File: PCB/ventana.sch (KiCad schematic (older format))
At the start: 55 parts, among them J1 Prog, J10 CLS, J2 SW1, J3 GND, J4 SW2, J5 GND, J6 VBat, J7 Motor+, J8 Motor-, J9 GND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

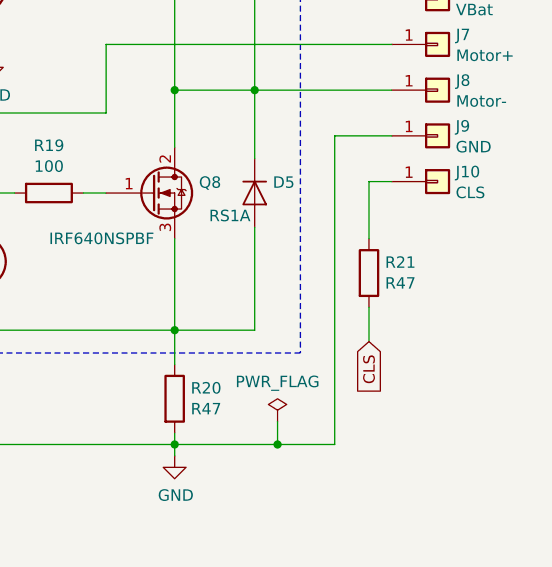
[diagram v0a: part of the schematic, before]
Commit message: Fixed a mistake in the schematic
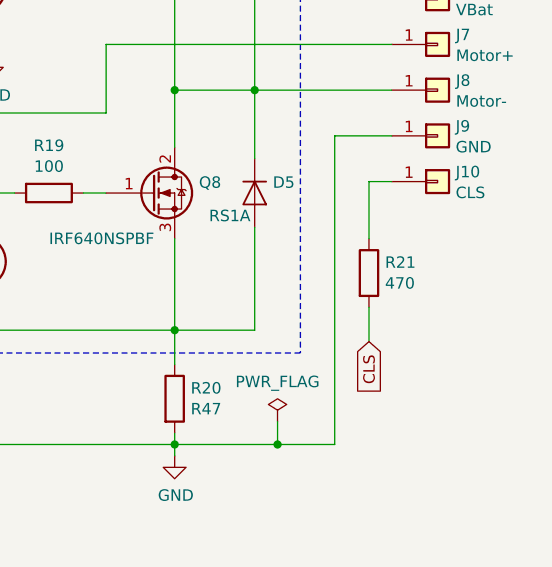
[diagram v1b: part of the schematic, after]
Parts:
- R21: value R47 -> 470
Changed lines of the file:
@@
 EESchema Schematic File Version 4
 LIBS:ventana-cache
-EELAYER 26 0
+EELAYER 29 0
 EELAYER END
 $Descr A4 11693 8268
@@
 P 10100 4450
 F 0 "R21" H 10170 4496 50  0000 L CNN
-F 1 "R47" H 10170 4405 50  0000 L CNN
+F 1 "470" H 10170 4405 50  0000 L CNN
 F 2 "Resistor_SMD:R_1206_3216Metric" V 10030 4450 50  0001 C CNN
 F 3 "~" H 10100 4450 50  0001 C CNN

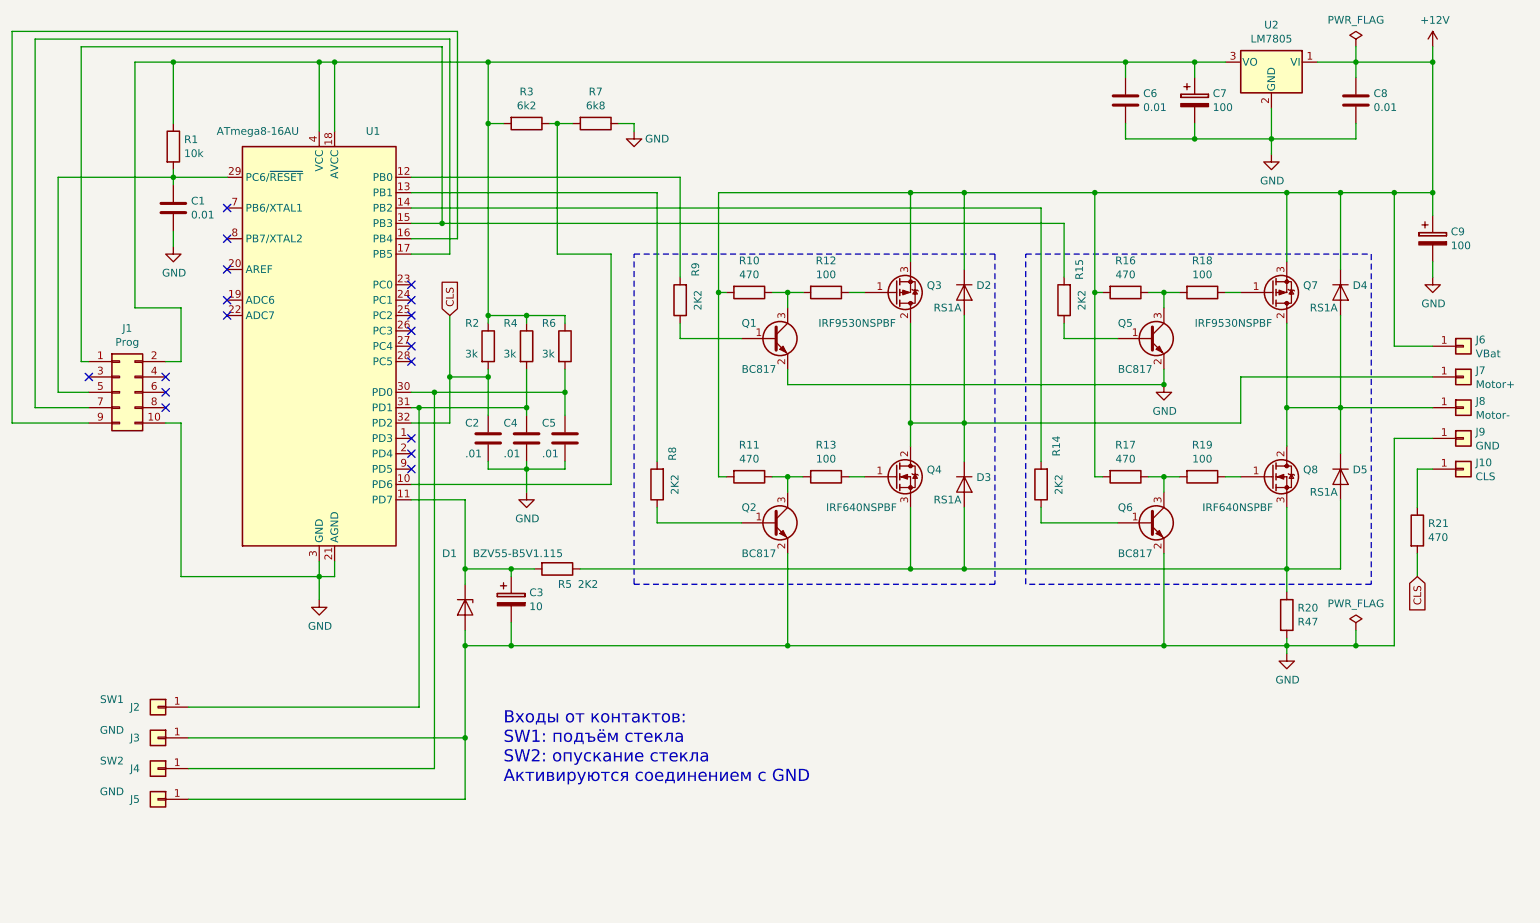
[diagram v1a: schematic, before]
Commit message: Load voltage sense circuits added to schematic
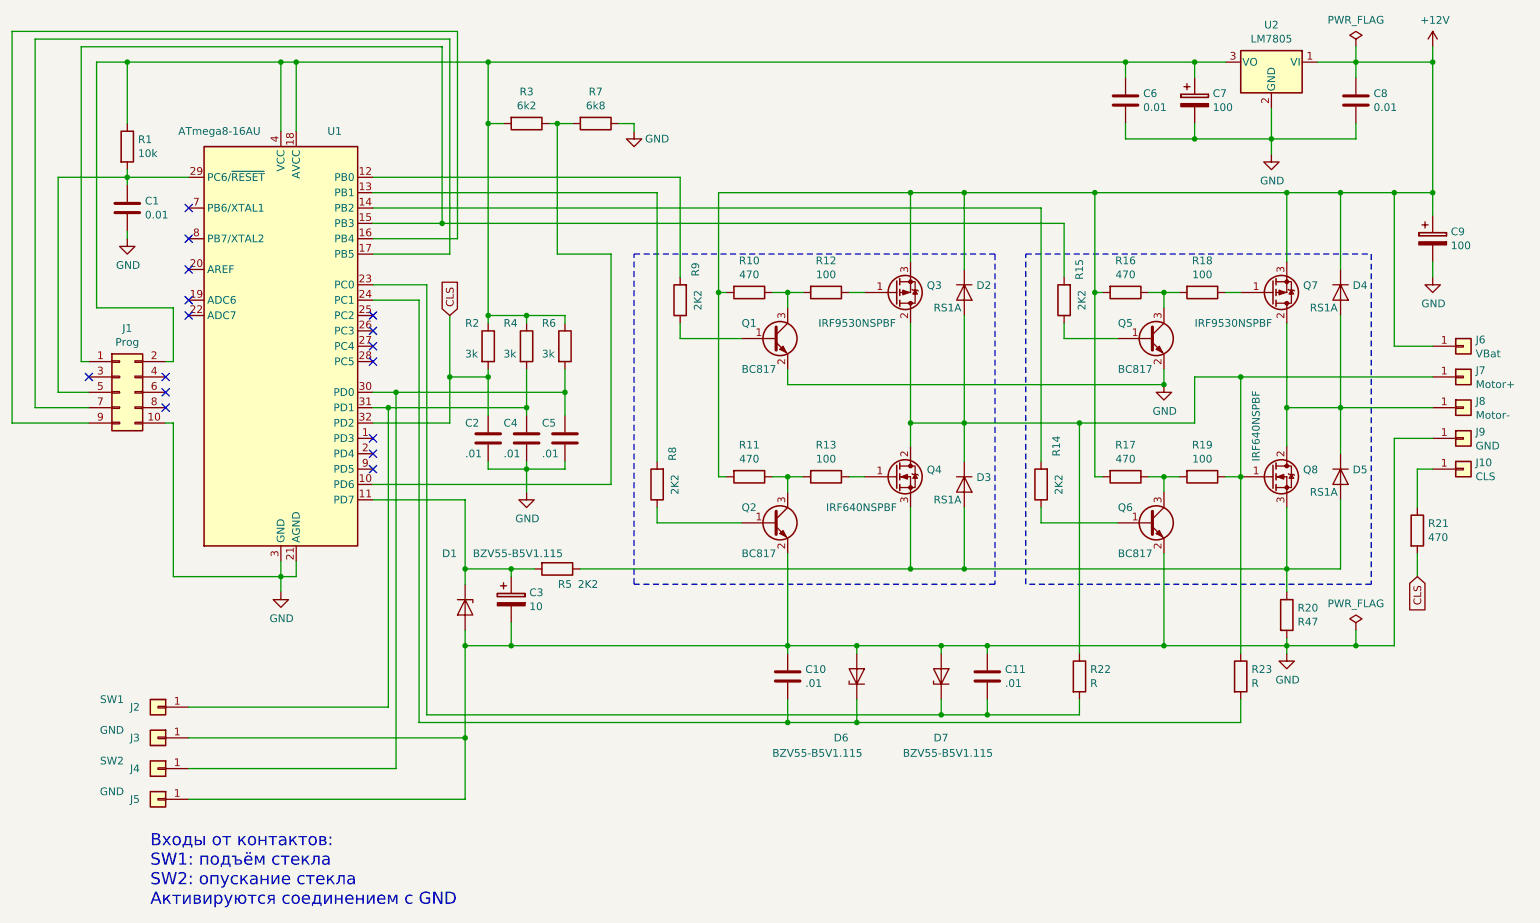
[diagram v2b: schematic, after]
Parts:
- added C10, C11: .01, Capacitor_SMD:C_1206_3216Metric, symbol Device:C
- added D6, D7: BZV55-B5V1.115, Diode_SMD:D_SOD-123, symbol Device:D_Zener
- added R22, R23: R, Resistor_SMD:R_1206_3216Metric, symbol Device:R
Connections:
- net GND: now also C10.1, C11.1, D6.2 (A), D7.2 (A)
- net at Q8.1 (G), R19.1: now also D2.2 (A), D3.1 (K), J7.1 (Pin_1), Q3.2 (D), Q4.2 (D), R22.1, R23.1
- net at U1.23 (PC0): now also C11.2, D7.1 (K), R22.2
- net at U1.24 (PC1): now also C10.2, D6.1 (K), R23.2
- no-connect marks 18 -> 16
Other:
- moved on the sheet: C1, R1, U1

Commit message: Schematic and PCB
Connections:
- net at D2.2 (A), D3.1 (K), J7.1 (Pin_1)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: no longer Q8.1 (G), R19.1
- new net: Q8.1 (G), R19.1
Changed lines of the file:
@@
 	8950 3450 10200 3450
-Wire Wire Line
-	8950 3450 8950 4100
 Wire Wire Line
 	7000 5250 7000 5200
@@
 	3600 5700 6000 5700
 Connection ~ 6450 5700
-Connection ~ 8950 4100
-Wire Wire Line
-	8950 4100 8950 5250
 $Comp
 L Device:C C11
@@
 Wire Wire Line
 	7300 5650 7000 5650
+Wire Wire Line
+	8950 3450 8950 5250
 $EndSCHEMATC

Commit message: Added parts for midpoints voltage measurement
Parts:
- added R24, R25, R26: R, Resistor_SMD:R_1206_3216Metric, symbol Device:R
- U2: value LM7805 -> LM2937; footprint Package_TO_SOT_SMD:TO-263-2 -> Package_TO_SOT_SMD:SOT-223; symbol Regulator_Linear:LM7805_TO220 -> Regulator_Linear:LM2937xMP
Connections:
- net GND: now also R24.1, R25.1
- net at D4.2 (A), D5.1 (K), J8.1 (Pin_1)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: now also R23.1
- net at D2.2 (A), D3.1 (K), J7.1 (Pin_1)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: no longer R23.1
- net at C5.1, R6.2, U1.30 (PD0): now also R26.1; no longer J4.1 (Pin_1)
- net at J1.1 (Pin_1), U1.15 (PB3): no longer R15.2
- net at C11.2, D7.1 (K), R22.2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: now also R24.2
- net at C10.2, D6.1 (K), R23.2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: now also R25.2
- net at U1.7 (PB6/XTAL1): now also R15.2
- new net: J4.1 (Pin_1), R26.2
- no-connect marks 16 -> 15
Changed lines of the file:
@@
 EESchema Schematic File Version 4
 LIBS:ventana-cache
-EELAYER 29 0
+EELAYER 26 0
 EELAYER END
 $Descr A4 11693 8268
@@
 P 9150 4100
 F 0 "Q8" H 9356 4146 50  0000 L CNN
-F 1 "IRF640NSPBF" V 9050 4200 50  0000 L CNN
+F 1 "IRF640NSPBF" V 9100 3550 50  0000 L CNN
 F 2 "Package_TO_SOT_SMD:TO-263-2" H 9350 4200 50  0001 C CNN
 F 3 "~" H 9150 4100 50  0001 C CNN
@@
 Connection ~ 8450 5200
 Wire Wire Line
-	8450 5200 9250 5200
+	8450 5200 8600 5200
 Wire Wire Line
 	9250 2250 8000 2250
@@
 Connection ~ 9950 2250
 $Comp
-L Regulator_Linear:LM7805_TO220 U2
+L Regulator_Linear:LM2937xMP U2
 U 1 1 5C0B6455
 P 9150 1400
 F 0 "U2" H 9150 1642 50  0000 C CNN
-F 1 "LM7805" H 9150 1551 50  0000 C CNN
-F 2 "Package_TO_SOT_SMD:TO-263-2" H 9150 1625 50  0001 C CIN
+F 1 "LM2937" H 9150 1551 50  0000 C CNN
+F 2 "Package_TO_SOT_SMD:SOT-223" H 9150 1625 50  0001 C CIN
 F 3 "http://www.fairchildsemi.com/ds/LM/LM7805.pdf" H 9150 1350 50  0001 C CNN
 	1    9150 1400
@@
 Wire Wire Line
 	8650 3750 8650 3450
-Wire Wire Line
-	8650 3450 8950 3450
 Connection ~ 6800 3750
 Wire Wire Line
@@
 	3400 5600 2100 5600
 Wire Wire Line
-	2100 6000 3450 6000
+	2100 6000 2800 6000
 Wire Wire Line
 	3450 3550 3300 3550
@@
 U 1 1 5C07337D
 P 1700 2350
-F 0 "C1" H 1815 2396 50  0000 L CNN
-F 1 "0.01" H 1815 2305 50  0000 L CNN
+F 0 "C1" H 1550 2250 50  0000 L CNN
+F 1 "0.01" H 1750 2250 50  0000 L CNN
 F 2 "Capacitor_SMD:C_1206_3216Metric" H 1738 2200 50  0001 C CNN
 F 3 "~" H 1700 2350 50  0001 C CNN
@@
 Wire Wire Line
 	1400 3350 1450 3350
-Connection ~ 3750 2450
-Wire Wire Line
-	3750 2450 7800 2450
 Wire Wire Line
 	1700 2150 1250 2150
@@
 NoConn ~ 3300 3250
 NoConn ~ 3300 3350
-NoConn ~ 2100 2350
 NoConn ~ 2100 2550
 NoConn ~ 2100 2750
@@
 Wire Wire Line
 	7900 3750 8650 3750
-Connection ~ 8950 3450
-Wire Wire Line
-	8950 3450 10200 3450
 Wire Wire Line
 	7000 5250 7000 5200
@@
 	8950 5550 8950 5700
 Wire Wire Line
-	8950 5700 6450 5700
+	8950 5700 8600 5700
 Wire Wire Line
 	6450 5700 6450 5550
@@
 Connection ~ 7300 5200
 Wire Wire Line
-	7300 5200 8450 5200
+	7300 5200 8250 5200
 Wire Wire Line
 	7300 5550 7300 5650
@@
 	7300 5650 7000 5650
 Wire Wire Line
-	8950 3450 8950 5250
+	2100 2350 1950 2350
+Wire Wire Line
+	1950 2350 1950 1150
+Wire Wire Line
+	1950 1150 3900 1150
+Wire Wire Line
+	3900 1150 3900 2450
+Wire Wire Line
+	3900 2450 7800 2450
+$Comp
+L Device:R R24
+U 1 1 5C25358B
+P 8250 5400
+F 0 "R24" H 8320 5446 50  0000 L CNN
+F 1 "R" H 8320 5355 50  0000 L CNN
+F 2 "Resistor_SMD:R_1206_3216Metric" V 8180 5400 50  0001 C CNN
+F 3 "~" H 8250 5400 50  0001 C CNN
+	1    8250 5400
+	1    0    0    -1
+$EndComp
+$Comp
+L Device:R R25
+U 1 1 5C2536A7
+P 8600 5400
+F 0 "R25" H 8670 5446 50  0000 L CNN
+F 1 "R" H 8670 5355 50  0000 L CNN
+F 2 "Resistor_SMD:R_1206_3216Metric" V 8530 5400 50  0001 C CNN
+F 3 "~" H 8600 5400 50  0001 C CNN
+	1    8600 5400
+	1    0    0    -1
+$EndComp
+Wire Wire Line
+	7900 5650 8250 5650
+Wire Wire Line
+	8250 5650 8250 5550
+Connection ~ 7900 5650
+Wire Wire Line
+	8600 5550 8600 5700
+Connection ~ 8600 5700
+Wire Wire Line
+	8600 5700 6450 5700
+Wire Wire Line
+	8600 5250 8600 5200
+Connection ~ 8600 5200
+Wire Wire Line
+	8600 5200 9250 5200
+Wire Wire Line
+	8250 5250 8250 5200
+Connection ~ 8250 5200
+Wire Wire Line
+	8250 5200 8450 5200
+Wire Wire Line
+	8650 3450 10200 3450
+Wire Wire Line
+	8950 3650 9250 3650
+Wire Wire Line
+	8950 3650 8950 5250
+$Comp
+L Device:R R26
+U 1 1 5C2ACA41
+P 2950 6000
+F 0 "R26" V 2850 5850 50  0000 C CNN
+F 1 "R" V 2834 6000 50  0000 C CNN
+F 2 "Resistor_SMD:R_1206_3216Metric" V 2880 6000 50  0001 C CNN
+F 3 "~" H 2950 6000 50  0001 C CNN
+	1    2950 6000
+	0    1    1    0
+$EndComp
+Wire Wire Line
+	3100 6000 3450 6000
 $EndSCHEMATC

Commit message: PCB rev 1.0b
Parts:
- added R27: R, Resistor_SMD:R_1206_3216Metric, symbol Device:R
- J1: footprint Connector_PinHeader_2.54mm:PinHeader_2x05_P2.54mm_Vertical -> Ventana:conn_2_5
- U1: footprint Package_QFP:TQFP-32_7x7mm_P0.8mm -> Ventana:AtMega8_TQFP32
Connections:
- net at C4.1, R4.2, U1.31 (PD1): now also R27.1; no longer J2.1 (Pin_1)
- new net: J2.1 (Pin_1), R27.2
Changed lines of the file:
@@
 F 0 "U1" H 3050 4650 50  0000 C CNN
 F 1 "ATmega8-16AU" H 2300 4650 50  0000 C CNN
-F 2 "Package_QFP:TQFP-32_7x7mm_P0.8mm" H 2700 3250 50  0001 C CIN
+F 2 "Ventana:AtMega8_TQFP32" H 2700 3250 50  0001 C CIN
 F 3 "http://ww1.microchip.com/downloads/en/DeviceDoc/atmel-2486-8-bit-avr-microcontroller-atmega8_l_datasheet.pdf" H 2700 3250 50  0001 C CNN
 	1    2700 3250
@@
 	3400 3650 3400 5600
 Wire Wire Line
-	3400 5600 2100 5600
+	3400 5600 3100 5600
 Wire Wire Line
 	2100 6000 2800 6000
@@
 F 0 "J1" H 1700 3967 50  0000 C CNN
 F 1 "Prog" H 1700 3876 50  0000 C CNN
-F 2 "Connector_PinHeader_2.54mm:PinHeader_2x05_P2.54mm_Vertical" H 1650 3550 50  0001 C CNN
+F 2 "Ventana:conn_2_5" H 1650 3550 50  0001 C CNN
 F 3 "~" H 1650 3550 50  0001 C CNN
 	1    1650 3550
@@
 Wire Wire Line
 	3100 6000 3450 6000
+$Comp
+L Device:R R27
+U 1 1 5C44EFD2
+P 2950 5600
+F 0 "R27" V 2743 5600 50  0000 C CNN
+F 1 "R" V 2834 5600 50  0000 C CNN
+F 2 "Resistor_SMD:R_1206_3216Metric" V 2880 5600 50  0001 C CNN
+F 3 "~" H 2950 5600 50  0001 C CNN
+	1    2950 5600
+	0    1    1    0
+$EndComp
+Wire Wire Line
+	2800 5600 2100 5600
 $EndSCHEMATC
